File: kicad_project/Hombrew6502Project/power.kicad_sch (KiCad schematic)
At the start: 48 parts, among them J501 +5VDC, U101 74HC04, U102 74HC74, U103 74HC74, U105 CD74HC4002M96, U106 SN74LS07, U107 74AHC2G00, U110 74AHC08D-Q100J, U501 LD1117STR, U502 LD1117S33TR_SOT223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

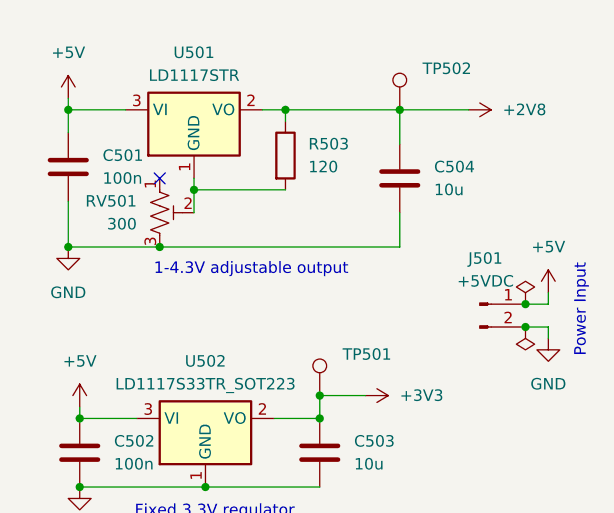
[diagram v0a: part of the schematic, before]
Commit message: footprint assignments and separate project for RAM board
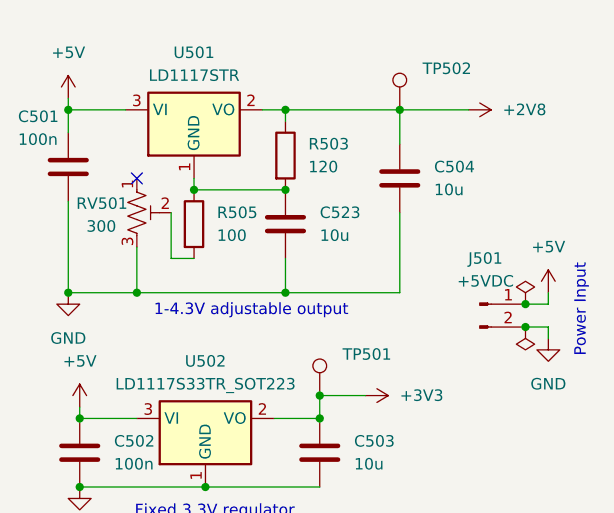
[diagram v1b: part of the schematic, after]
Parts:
- added C523: 10u, Capacitor_SMD:C_0402_1005Metric, symbol Device:C
- added R505: 100, Resistor_SMD:R_0402_1005Metric, symbol Device:R
- J501: footprint (none) -> Connector_PinHeader_2.54mm:PinHeader_1x02_P2.54mm_Vertical
- RV501: footprint (none) -> Potentiometer_SMD:Potentiometer_Bourns_TC33X_Vertical
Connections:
- net GND: now also C523.2
- net at R503.2, U501.1 (GND): now also C523.1, R505.1; no longer RV501.2
- new net: R505.2, RV501.2
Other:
- moved on the sheet: RV501

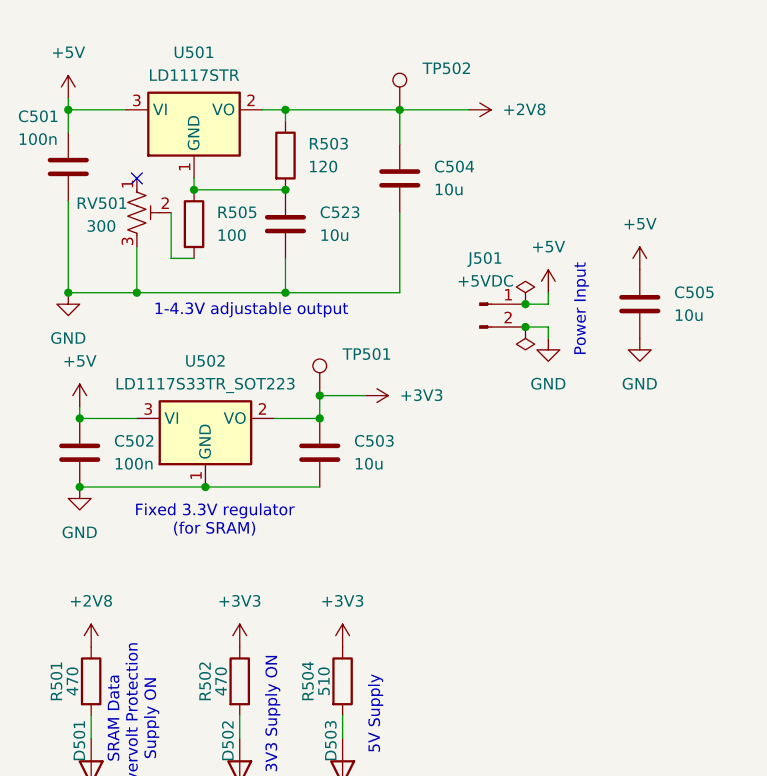
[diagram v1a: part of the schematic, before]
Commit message: Peripheral io layout done; snapshot of current state before redoing much of the rest of the layout.
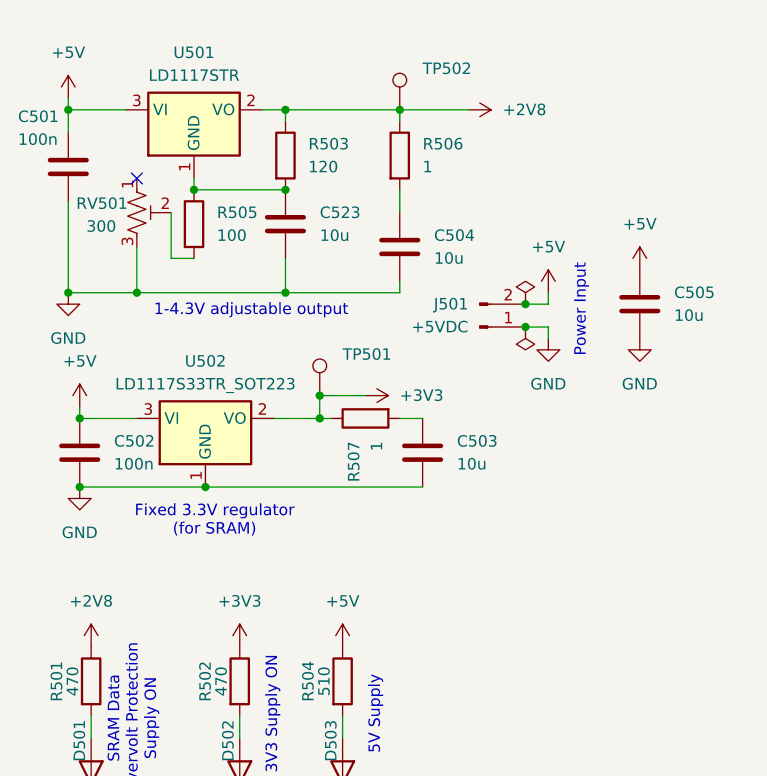
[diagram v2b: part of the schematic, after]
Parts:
- added R506, R507: 1, Resistor_SMD:R_0402_1005Metric, symbol Device:R
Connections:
- net +2V8: now also R506.1; no longer C504.1
- net +3V3: now also R507.1; no longer C503.1, R504.1
- net +5V: now also J501.2 (Pin_2), R504.1; no longer J501.1 (Pin_1)
- net GND: now also J501.1 (Pin_1); no longer J501.2 (Pin_2)
- new net: C504.1, R506.2
- new net: C503.1, R507.2
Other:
- moved on the sheet: C503, C504
